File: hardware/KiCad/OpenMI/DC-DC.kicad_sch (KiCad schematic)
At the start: 33 parts, among them Q4 GAN7R0-150LBEZ, Q5 GAN7R0-150LBEZ, U3 1EDN7550B, U4 1EDN7550B

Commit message: docs(hw): adds first considerations for transformer (WIP)
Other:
- note added: "TODO: Clamping Diodes to make sure GaN FET limit (currently 150V) is met"
- note added: "TODO: Do we use voltage doubler circuit consisting of 2 capacitors? If not, we probably have turn ratio of about ≈ 5 Double check equation 7 from AN4070: Why 0.2 instead of 0.7?"
- note added: "The inductors (= boost converter) create a rise of voltage of V_{out} = V_{in} * 1 / (1 - D), where 0.5 < D ≤ 0.7. Therefore, if we consider V_{in,min} = 30 V. V_{out,V_{in,min}} = 30 V / (1 - 0.5) = 60 V V_{out,V_{in,min}} = 30 V / (1 - 0.7) = 100 V For the ΔV = 40V (might be changed to 50V) => V_{bus,min} = 360V; V_{bus,max} = 400V If we take the same transformer specifications as in AN4070: N_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"
- note added: "Transformer"
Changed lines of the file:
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@@
+    (fill (type none))
+  )
+  (rectangle (start 138.43 163.83) (end 299.72 242.57)
+    (stroke (width 0) (type default))
     (fill (type none))
   )
@@
     (effects (font (size 1.27 1.27)) (justify left bottom))
   )
+  (text "TODO:\nClamping Diodes to make sure\nGaN FET limit (currently 150V) is met"
+    (at 320.04 151.13 0)
+    (effects (font (size 1.27 1.27) bold (color 255 0 0 1)) (justify left bottom))
+  )
   (text "The GAN7R0-150LBEZ has a input capacitance of \n C_{iss} = 865 pF\nThe gate driver 1EDN7550B has rise times of\n t_{rise_1.8nF} = 6.5 ns\n t_{rise_200pF} = 1 ns\nSo using the GAN7R0-150LBEZ with the 1EDN7550B we can roughly asume:\n t_{rise_865pf} = (6.5 ns - 1 ns) / (1800 pF - 200 pF) * 865 pF  \n            = 2.97 ns\nThis results in\n  t_{charge_QGS} = 2.97 ns + 1.7 nC / 4 A  = 3.395 ns,\nwhich is\n  t_{charge_QGS} / T_{on_minimal} = 3.395 ns / 2000 ns ≈ 0.0017,\nso the rise time is at maximum 0.17% of the period time.\nThe results for the fall time should be roughly similar.\n\nSimulating this in LTSpice with\n  R_{Gate_SNK} = 2.2 Ω\n  R_{Gate_SRC} = 0.5 Ω\nresults in the following times (measuring V_{GS} from 10% to 90%)\n  t_{charge_QGS} = 8.44 ns     → 0.42% of period time\n  t_{discharge_QGS} = 2.59 ns   → 0.13% of period time"
     (at 142.24 133.35 0)
@@
     (effects (font (size 1.27 1.27)) (justify left bottom))
   )
+  (text "Transformer" (at 140.97 168.91 0)
+    (effects (font (size 2 2) bold) (justify left bottom))
+  )
   (text "C_{in, nominal} ≥ 2 * C_{boost}\n            ≥ 1.4 uF\n"
     (at 22.86 40.005 0)
@@
     (effects (font (size 1.27 1.27)) (justify left bottom))
   )
+  (text "The inductors (= boost converter) create a rise of voltage of\n  V_{out} = V_{in} * 1 / (1 - D),\nwhere 0.5 < D ≤ 0.7.\nTherefore, if we consider V_{in,min} = 30 V.\n  V_{out,V_{in,min}} = 30 V / (1 - 0.5) = 60 V  \n  V_{out,V_{in,min}} = 30 V / (1 - 0.7) = 100 V\n\nFor the ΔV = 40V (might be changed to 50V) => V_{bus,min} = 360V; V_{bus,max} = 400V\n\nIf we take the same transformer specifications as in AN4070:\n  N_{2} / N_{1} = V_{2} / V_{1} = 2.6\n  V_{2} = V_{bus}\n\n  -> V_{1,max} = V_{bus,max} / 2.6 = 400 V / 2.6 = 153.85 V\n  -> V_{1,min} = V_{bus,min} / 2.6 = 360 V / 2.6 = 138.46 V "
+    (at 143.51 201.93 0)
+    (effects (font (size 1.27 1.27)) (justify left bottom))
+  )
+  (text "TODO:\nDo we use voltage doubler circuit consisting of 2 capacitors? If not, we probably have turn ratio of about ≈ 5\nDouble check equation 7 from AN4070: Why 0.2 instead of 0.7? \n"
+    (at 143.51 218.44 0)
+    (effects (font (size 1.27 1.27) (color 255 0 0 1)) (justify left bottom))
+  )
   (label "PWM_{GAN_2}-" (at 266.7 95.25 0) (fields_autoplaced)

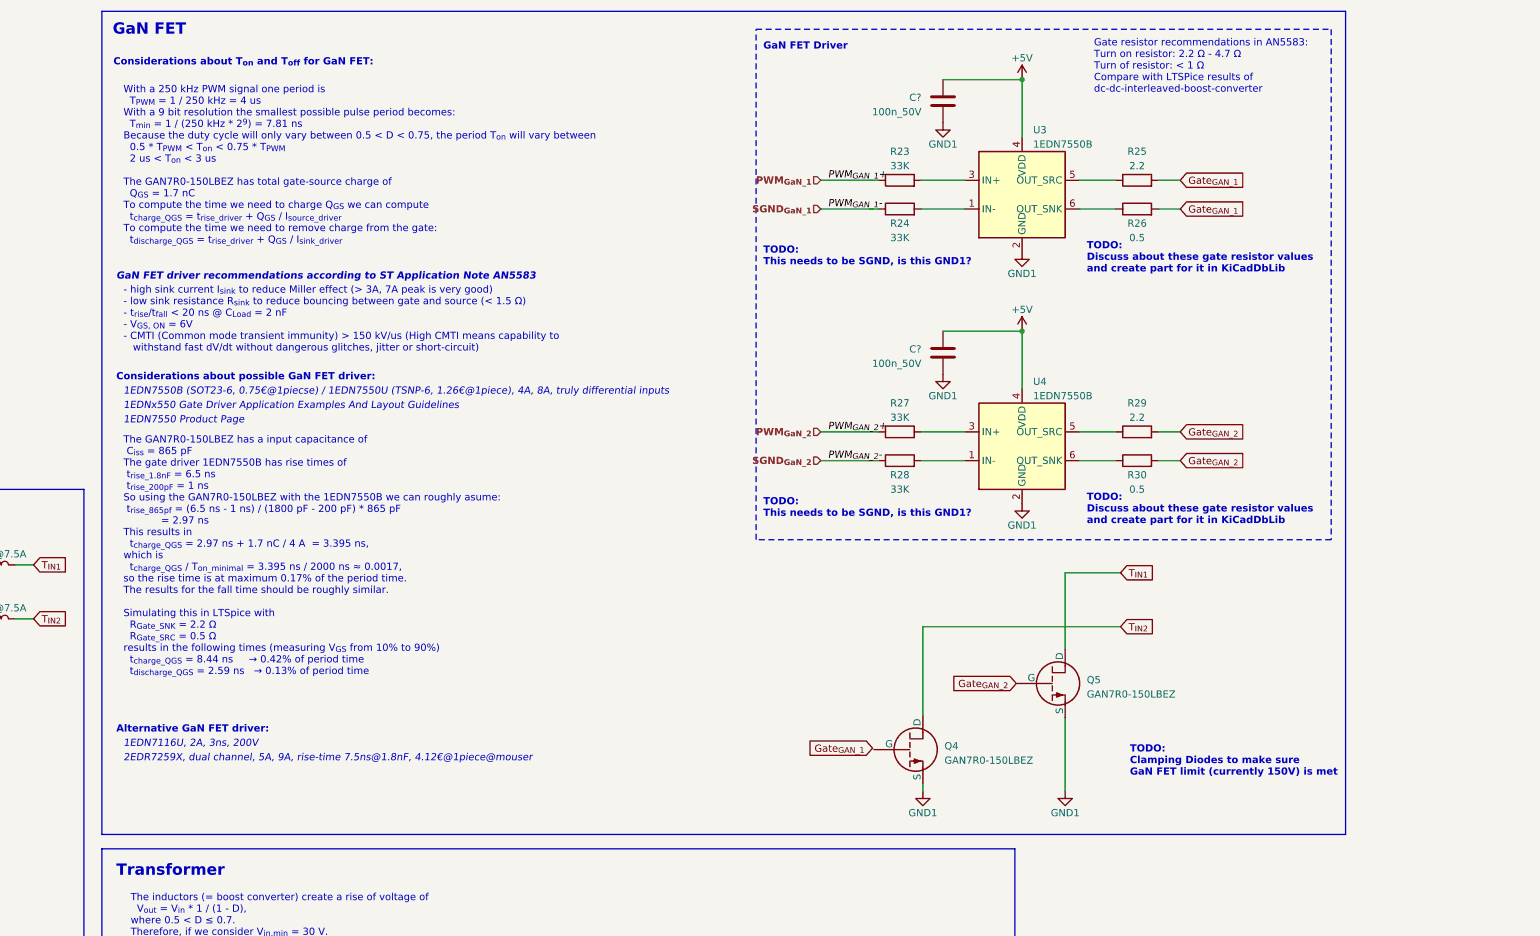
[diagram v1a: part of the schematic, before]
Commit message: feat(hw): adds resistors and capacitors from DbLib to GaN FET driver
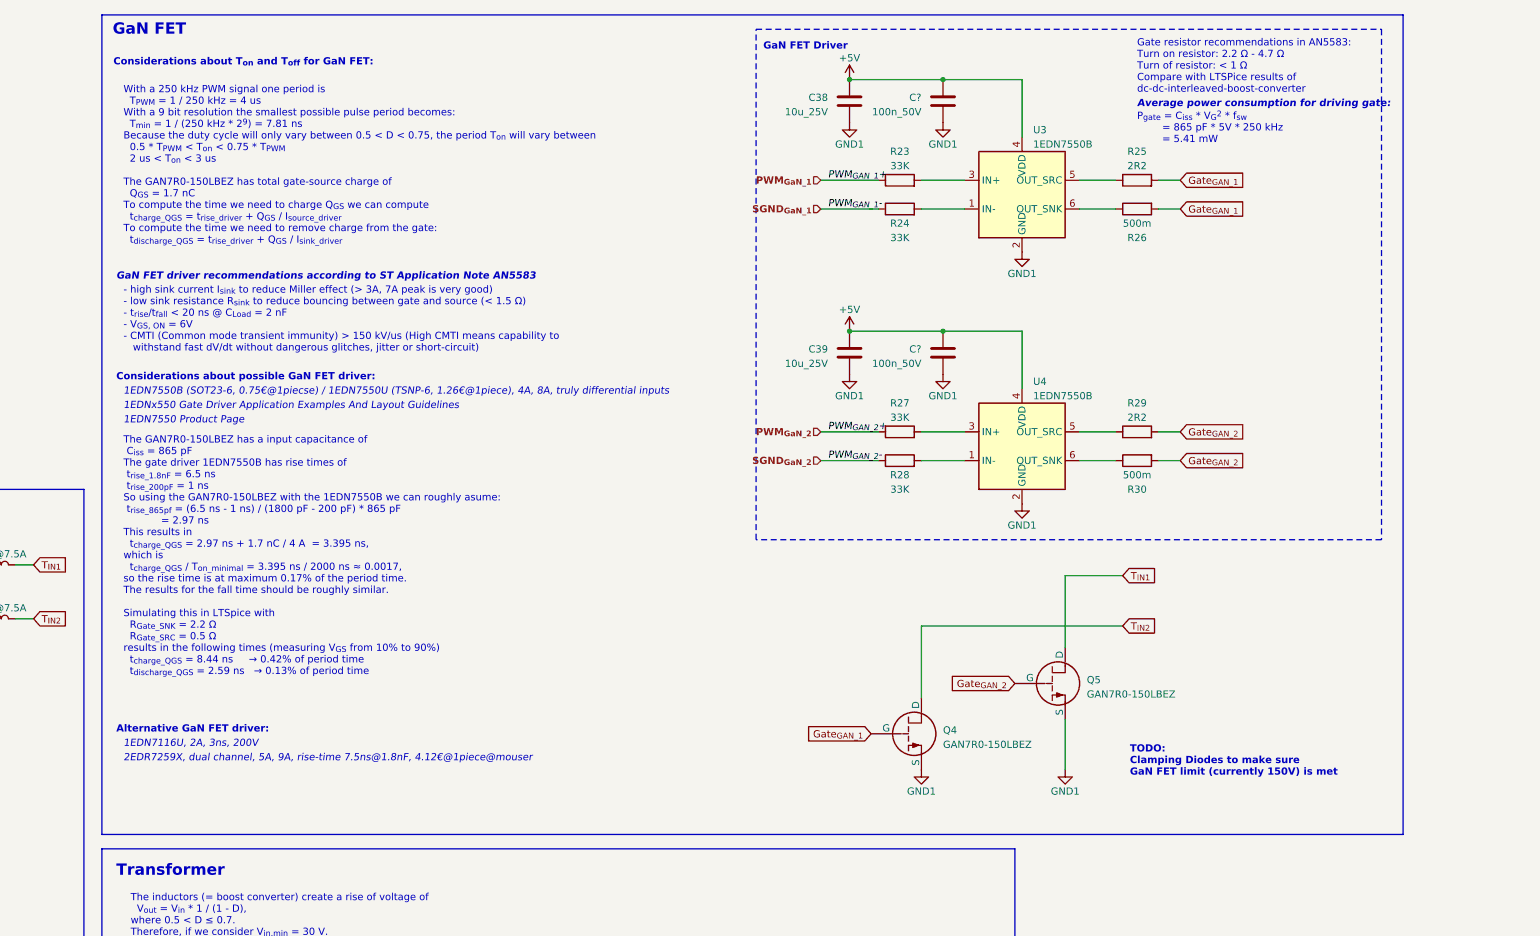
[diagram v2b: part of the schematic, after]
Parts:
- removed R25, R29: 2.2, Resistor_SMD:R_0603_1608Metric, symbol _R_0603:33K
- removed R26, R30: 0.5, Resistor_SMD:R_0603_1608Metric, symbol _R_0603:33K
- added C38, C39: 10u_25V, Capacitor_SMD:C_0805_2012Metric, symbol _C_0805:10u_25V
- added R25, R29: 2R2, Resistor_SMD:R_0603_1608Metric, symbol _R_0603:2R2
- added R26, R30: 500m, Resistor_SMD:R_0603_1608Metric, symbol _R_0603:500m
- R23, R24, R27, R28: MF YAGEO -> UNI-ROYAL; MPN RT0603BRD0733KL -> 0603WAF3302T5E; OC_LCSC (none) -> C4216
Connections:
- net +5V: now also C38.1, C39.1
- net GND1: now also C38.2, C39.2
- net Gate_{GAN_1}: now also Q4.2 (G), R25.2, R26.2
- net Gate_{GAN_2}: now also R29.2, R30.2
- net at U4.6 (OUT_SNK): now also R30.1
- net at U3.5 (OUT_SRC): now also R25.1
- net at U3.6 (OUT_SNK): now also R26.1
- net at U4.5 (OUT_SRC): now also R29.1
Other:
- note added: "Average power consumption for driving gate:"
- note added: "P_{gate} = C_{iss} * V_{G}^{2} * f_{sw} = 865 pF * 5V * 250 kHz = 5.41 mW"
- note removed: "TODO: Discuss about these gate resistor values and create part for it in KiCadDbLib"
- note removed: "TODO: This needs to be SGND, is this GND1?"

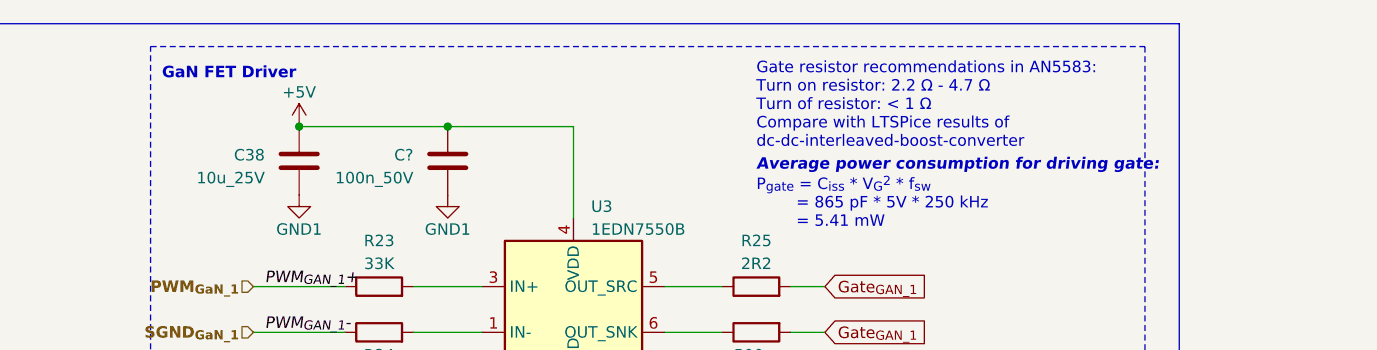
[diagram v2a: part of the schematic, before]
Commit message: docs(hw): adds link for source of gate resistor recommendations
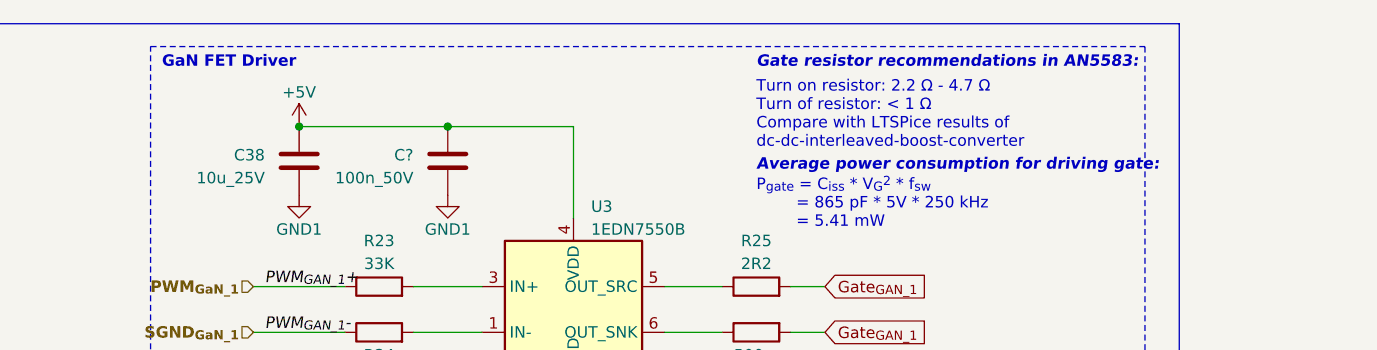
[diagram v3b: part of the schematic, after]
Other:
- note added: "Gate resistor recommendations in AN5583:"
- note added: "Turn on resistor: 2.2 Ω - 4.7 Ω Turn of resistor: < 1 Ω Compare with LTSPice results of dc-dc-interleaved-boost-converter"
- note removed: "Gate resistor recommendations in AN5583: Turn on resistor: 2.2 Ω - 4.7 Ω Turn of resistor: < 1 Ω Compare with LTSPice results of dc-dc-interleaved-boost-converter"
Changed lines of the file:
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@@
     (effects (font (size 1.27 1.27) italic) (justify left bottom) (href "https://www.infineon.com/dgdl/Infineon-DS_1EDN71X6U_2.0-DataSheet-v01_00-EN.pdf?fileId=8ac78c8c82af846e0182c6ff82134ec0"))
   )
-  (text "Gate resistor recommendations in AN5583:\nTurn on resistor: 2.2 Ω - 4.7 Ω\nTurn of resistor: < 1 Ω\nCompare with LTSPice results of\ndc-dc-interleaved-boost-converter"
+  (text "Turn on resistor: 2.2 Ω - 4.7 Ω\nTurn of resistor: < 1 Ω\nCompare with LTSPice results of\ndc-dc-interleaved-boost-converter"
     (at 321.31 30.48 0)
     (effects (font (size 1.27 1.27)) (justify left bottom))
@@
     (effects (font (size 1.27 1.27)) (justify left bottom))
   )
-  (text "GaN FET Driver" (at 255.27 22.86 0)
+  (text "GaN FET Driver" (at 255.27 21.59 0)
     (effects (font (size 1.27 1.27) bold) (justify left bottom))
   )
@@
     (effects (font (size 2 2) bold) (justify left bottom))
   )
+  (text "Gate resistor recommendations in AN5583:" (at 321.31 21.59 0)
+    (effects (font (size 1.27 1.27) (thickness 0.254) bold italic) (justify left bottom) (href "https://www.google.com/url?sa=t&rct=j&q=&esrc=s&source=web&cd=&cad=rja&uact=8&ved=2ahUKEwjewsbPm4eAAxWbQ6QEHfCnC8wQFnoECBAQAQ&url=https%3A%2F%2Fwww.st.com%2Fresource%2Fen%2Fapplication_note%2Fan5583-emode-gan-technology-tips-for-best-driving-stmicroelectronics.pdf&usg=AOvVaw1633zDZBu1lhtb6NTYWrBm&opi=89978449"))
+  )
   (text "C_{in, nominal} ≥ 2 * C_{boost}\n            ≥ 1.4 uF\n"

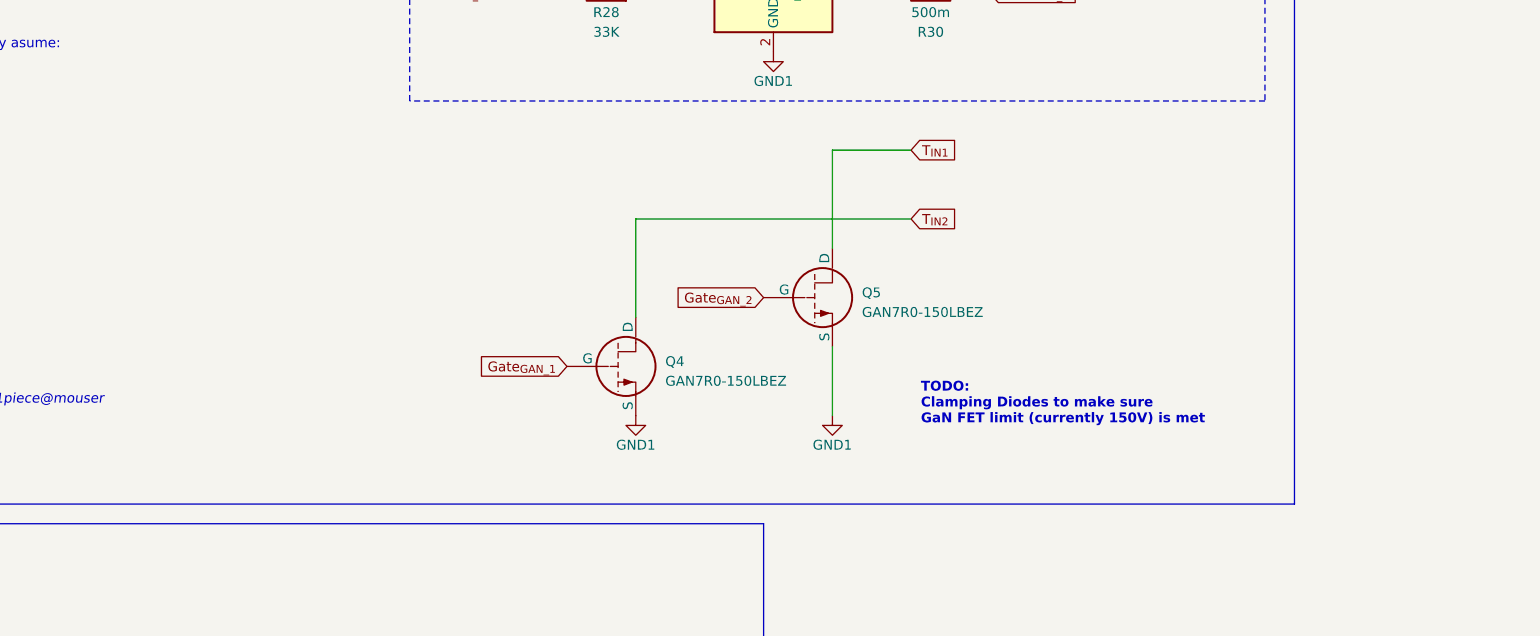
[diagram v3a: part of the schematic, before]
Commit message: feat(hw): adds protection diodes to GaN FET
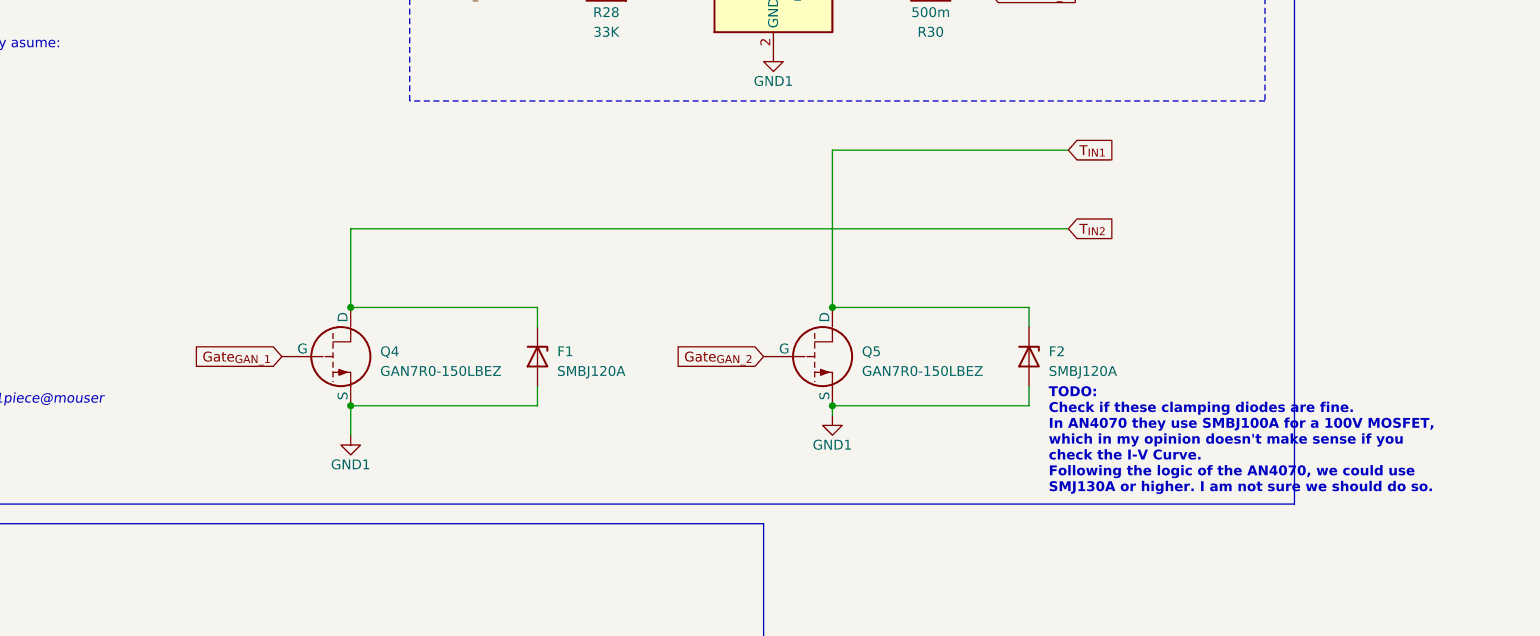
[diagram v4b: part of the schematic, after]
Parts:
- added F1, F2: SMBJ120A, Diode_SMD:D_SMB, symbol _Diode_TVS:SMBJ120A
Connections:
- net GND1: now also F1.2 (A), F2.2 (A)
- net T_{IN1}: now also F2.1 (K)
- net T_{IN2}: now also F1.1 (K)
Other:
- note added: "TODO: Check if these clamping diodes are fine. In AN4070 they use SMBJ100A for a 100V MOSFET, which in my opinion doesn't make sense if you check the I-V Curve. Following the logic of the AN4070, we could use SMJ130A or higher. I am not sure we should do so."
- note removed: "TODO: Clamping Diodes to make sure GaN FET limit (currently 150V) is met"
- moved on the sheet: Q4, Q5

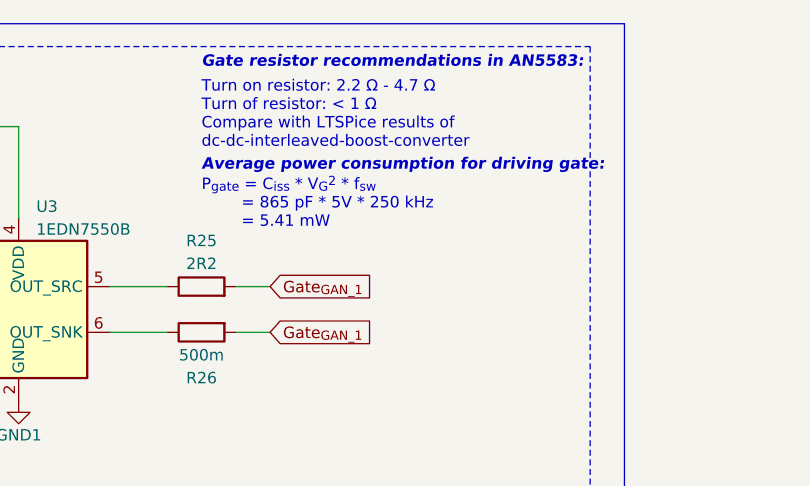
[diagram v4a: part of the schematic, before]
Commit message: docs(hw): fixing calculation intermediate step for power consumption of GaN FET gate
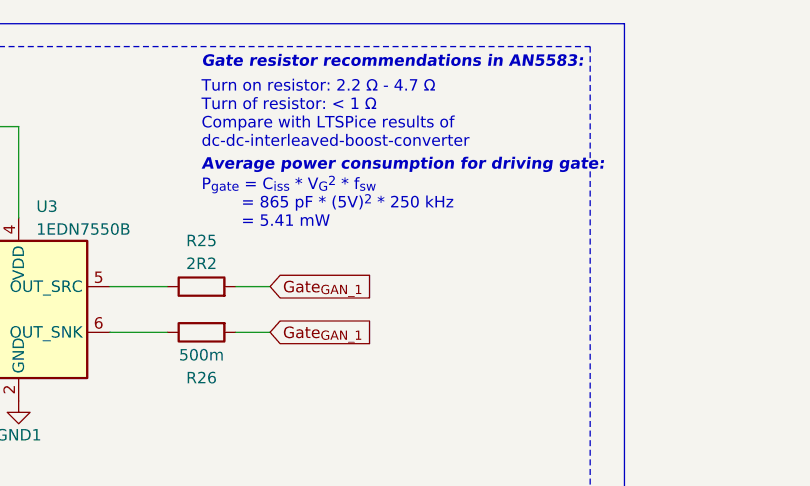
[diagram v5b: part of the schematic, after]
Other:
- note added: "P_{gate} = C_{iss} * V_{G}^{2} * f_{sw} = 865 pF * (5V)^{2} * 250 kHz = 5.41 mW"
- note removed: "P_{gate} = C_{iss} * V_{G}^{2} * f_{sw} = 865 pF * 5V * 250 kHz = 5.41 mW"
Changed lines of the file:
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@@
     (effects (font (size 1.27 1.27) bold) (justify left bottom))
   )
-  (text "P_{gate} = C_{iss} * V_{G}^{2} * f_{sw}\n        = 865 pF * 5V * 250 kHz\n        = 5.41 mW"
+  (text "P_{gate} = C_{iss} * V_{G}^{2} * f_{sw}\n        = 865 pF * (5V)^{2} * 250 kHz\n        = 5.41 mW"
     (at 321.31 39.37 0)
     (effects (font (size 1.27 1.27)) (justify left bottom))
